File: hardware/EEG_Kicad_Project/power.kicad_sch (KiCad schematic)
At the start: 0 parts

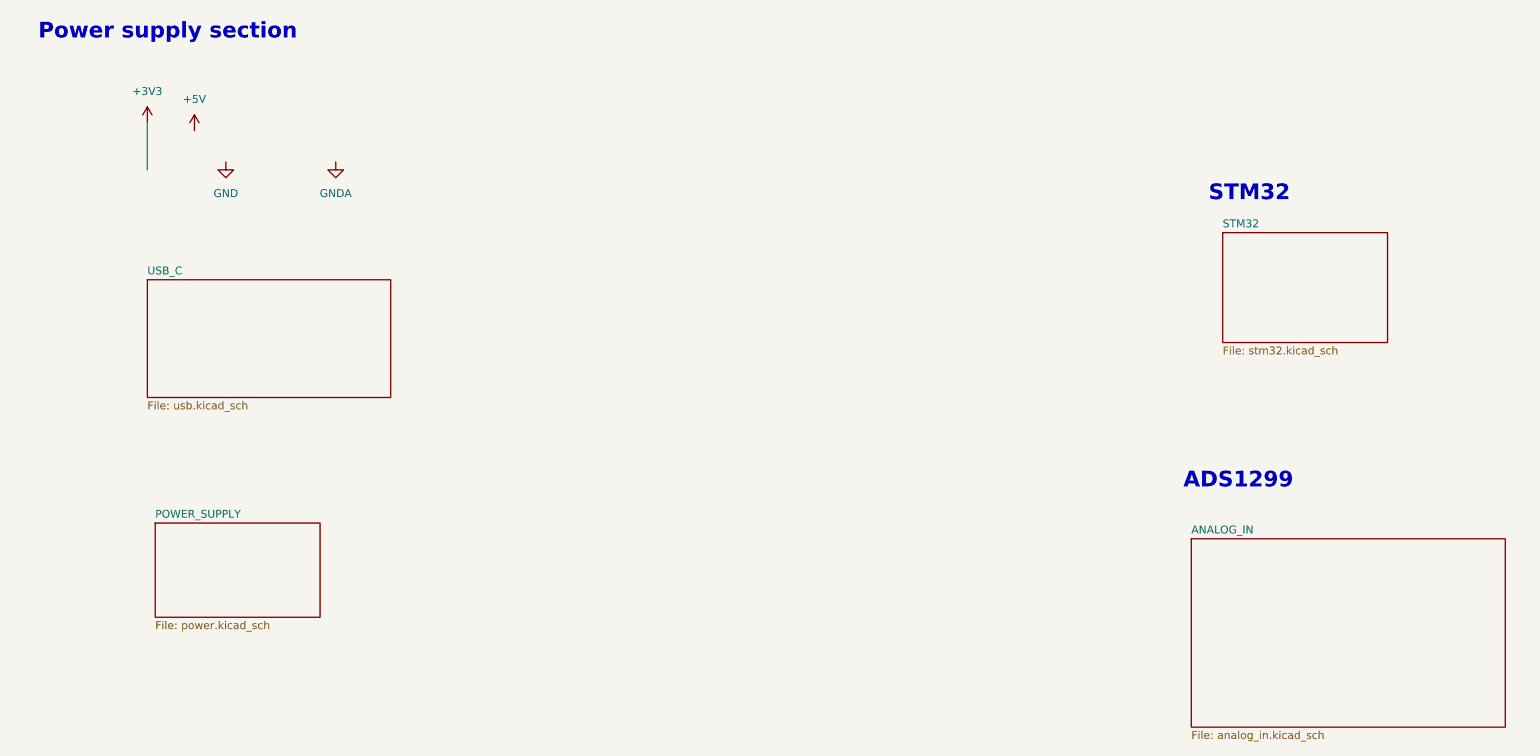
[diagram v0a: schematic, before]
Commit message: Added ADS1299, hierarchical sheets for: power, usb, analog, stm
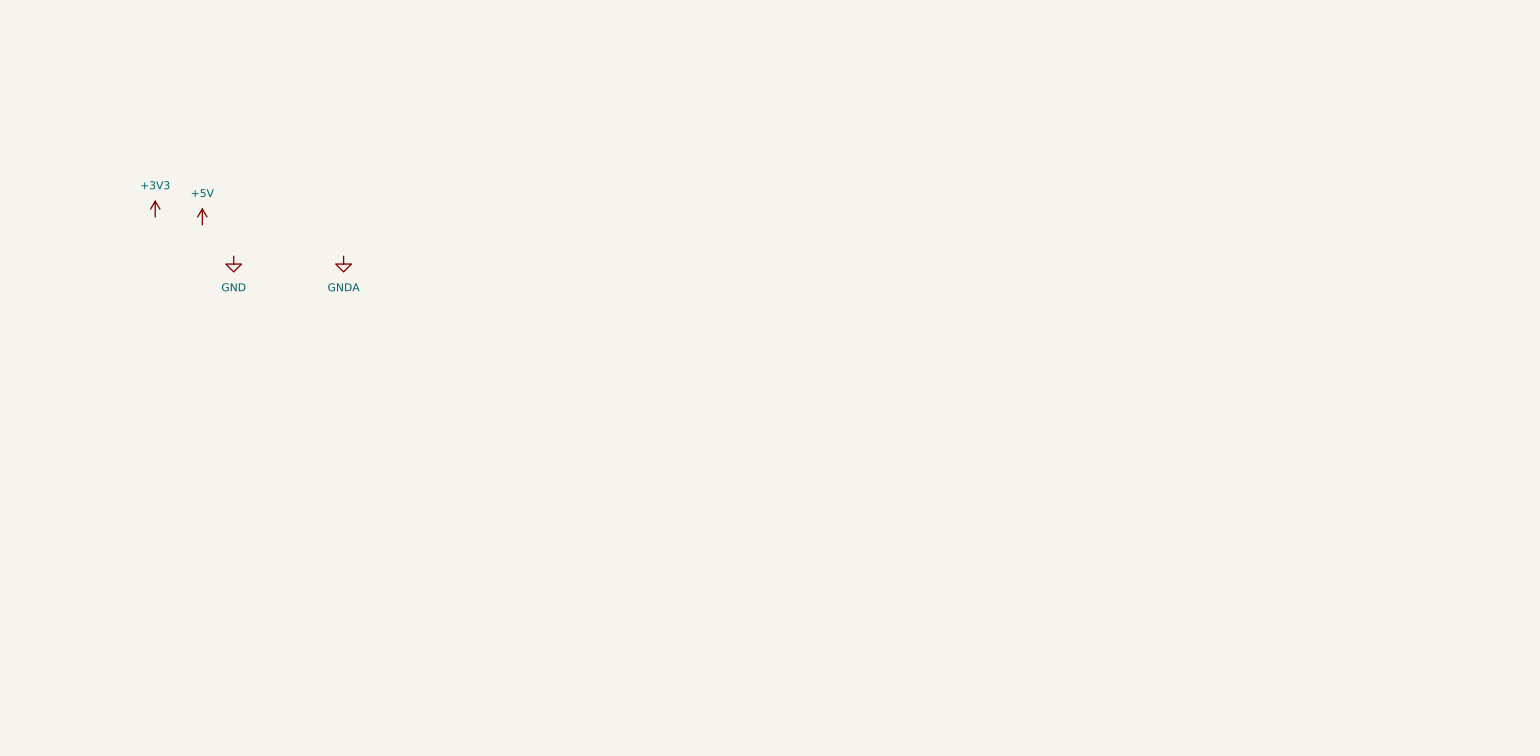
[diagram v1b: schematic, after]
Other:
- removed sheet ANALOG_IN
- removed sheet POWER_SUPPLY
- removed sheet STM32
- removed sheet USB_C
- note removed: "ADS1299"
- note removed: "Power supply section"
- note removed: "STM32"

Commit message: Readme change, add -5V, some organizational changes
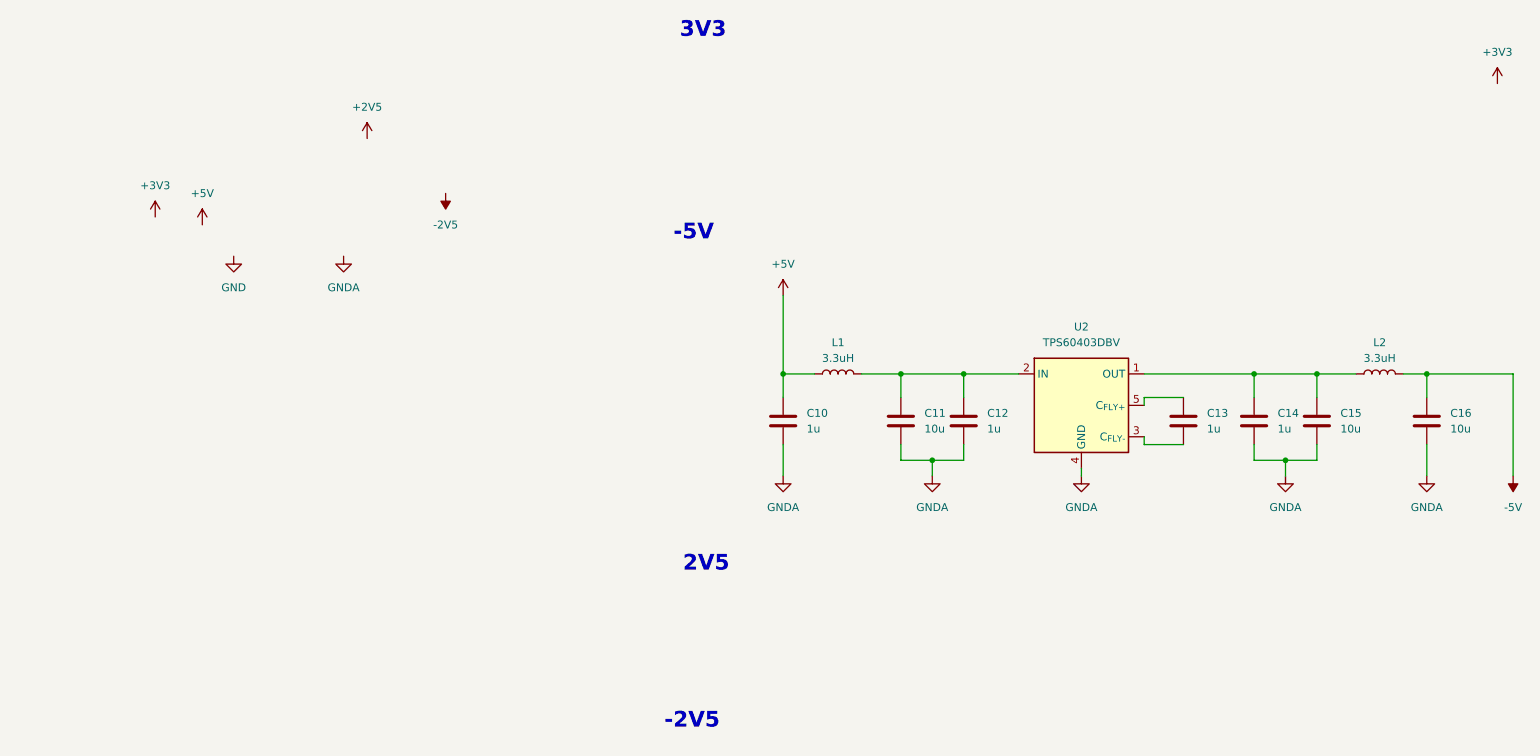
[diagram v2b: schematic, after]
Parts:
- added C10, C12, C13, C14: 1u, Capacitor_SMD:C_0603_1608Metric, symbol Device:C
- added C11, C15, C16: 10u, Capacitor_SMD:C_0603_1608Metric, symbol Device:C
- added L1, L2: 3.3uH, symbol Device:L
- added U2: TPS60403DBV, Package_TO_SOT_SMD:SOT-23-5, symbol Regulator_SwitchedCapacitor:TPS60403DBV
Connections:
- net +5V: now also C10.1, L1.1
- net GNDA: now also C10.2, C11.2, C12.2, C14.2, C15.2, C16.2, U2.4 (GND)
- new net: C13.1, U2.5 (C_{FLY+})
- new net: C13.2, U2.3 (C_{FLY-})
- new net: C14.1, C15.1, L2.1, U2.1 (OUT)
- new net: C11.1, C12.1, L1.2, U2.2 (IN)
- new net -5V: C16.1, L2.2
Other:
- note added: "-2V5"
- note added: "-5V"
- note added: "2V5"
- note added: "3V3"
